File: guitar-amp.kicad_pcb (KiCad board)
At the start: 2 copper layers, 41 parts, among them U1 ECC81, U2 ECC81, U3 EL84

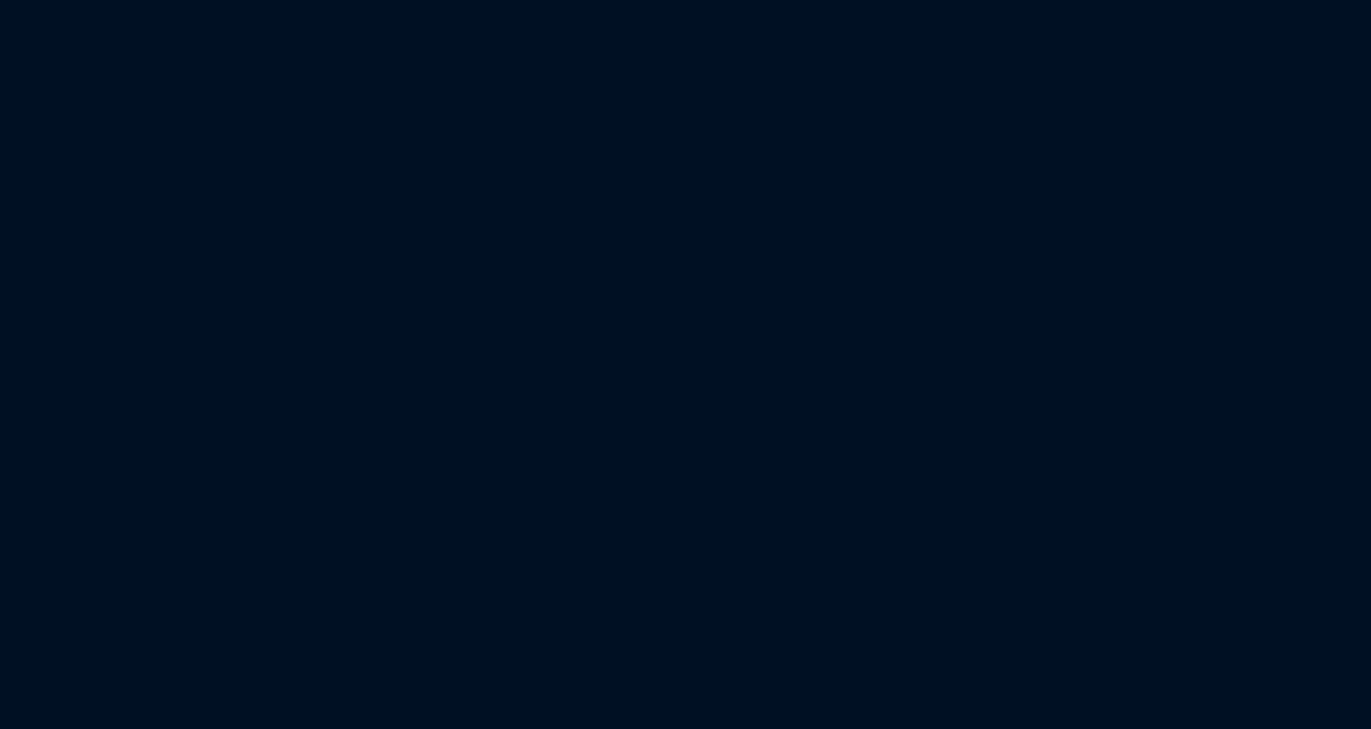
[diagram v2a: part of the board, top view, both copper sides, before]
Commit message: Add potentiometers
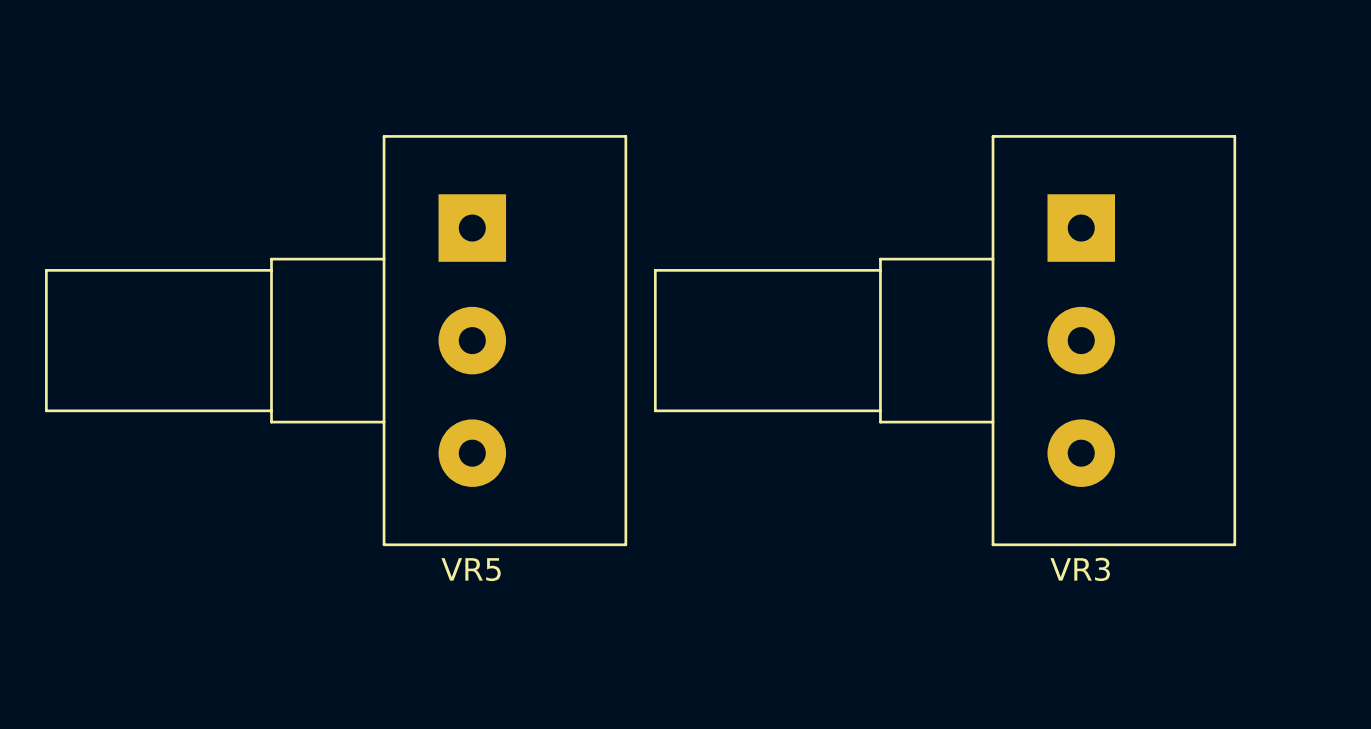
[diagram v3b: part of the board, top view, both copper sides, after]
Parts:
- added VR3: 220k LIN, Potentiometer_THT:Potentiometer_Alps_RK163_Single_Horizontal, F.Cu at (65.0, 70.0)
- added VR5: 25k LIN, Potentiometer_THT:Potentiometer_Alps_RK163_Single_Horizontal, F.Cu at (38.0, 70.0)
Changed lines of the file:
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@@
   (net 99 "unconnected-(C15-Pad1)")
   (net 100 "unconnected-(C15-Pad2)")
+  (net 101 "unconnected-(VR3-Pad1)")
+  (net 102 "unconnected-(VR3-Pad2)")
+  (net 103 "unconnected-(VR3-Pad3)")
+  (net 104 "unconnected-(VR5-Pad1)")
+  (net 105 "unconnected-(VR5-Pad2)")
+  (net 106 "unconnected-(VR5-Pad3)")
   (footprint "Resistor_THT:R_Axial_DIN0207_L6.3mm_D2.5mm_P7.62mm_Horizontal" (layer "F.Cu")
     (at 46.6 45.65)
@@
       (net 36 "unconnected-(R6-Pad2)") (pintype "passive"))
     (model "${KICAD6_3DMODEL_DIR}/Resistor_THT.3dshapes/R_Axial_DIN0207_L6.3mm_D2.5mm_P7.62mm_Horizontal.wrl"
+      (offset (xyz 0 0 0))
+      (scale (xyz 1 1 1))
+      (rotate (xyz 0 0 0))
+    )
+  )
+  (footprint "Potentiometer_THT:Potentiometer_Alps_RK163_Single_Horizontal" (layer "F.Cu")
+    (at 65 70)
+    (descr "1110U1Q 1110TNP 1110U2A 1110U0Q Potentiometer, horizontal, Alps RK163 Single, https://tech.alpsalpine.com/prod/e/pdf/potentiometer/rotarypotentiometers/rk16/rk16.pdf")
+    (tags "Potentiometer horizontal Alps RK163 Single")
+    (property "Sheetfile" "guitar-amp.kicad_sch")
+    (property "Sheetname" "")
+    (attr through_hole)
+    (fp_text reference "VR3" (at 0 15.2 180) (layer "F.SilkS")
+      (effects (font (size 1 1) (thickness 0.15)))
+    )
+    (fp_text value "220k LIN" (at 0 -5.200001 180) (layer "F.Fab")
+      (effects (font (size 1 1) (thickness 0.15)))
+    )
+    (fp_text user "${REFERENCE}" (at 1.45 4.999999 180) (layer "F.Fab")
+      (effects (font (size 1 1) (thickness 0.15)))
+    )
+    (fp_line (start -3.92 1.38) (end -8.92 1.38) (layer "F.SilkS") (width 0.12))
+    (fp_line (start -8.92 1.88) (end -18.92 1.88) (layer "F.SilkS") (width 0.12))
+    (fp_line (start 6.82 14.07) (end 6.82 -4.07) (layer "F.SilkS") (width 0.12))
+    (fp_line (start -3.92 14.07) (end -3.92 -4.07) (layer "F.SilkS") (width 0.12))
+    (fp_line (start -3.92 8.62) (end -8.92 8.62) (layer "F.SilkS") (width 0.12))
+    (fp_line (start 6.82 14.07) (end -3.92 14.07) (layer "F.SilkS") (width 0.12))
+    (fp_line (start -18.92 8.12) (end -18.92 1.88) (layer "F.SilkS") (width 0.12))
+    (fp_line (start -8.92 8.12) (end -18.92 8.12) (layer "F.SilkS") (width 0.12))
+    (fp_line (start 6.82 -4.07) (end -3.92 -4.07) (layer "F.SilkS") (width 0.12))
+    (fp_line (start -8.92 8.62) (end -8.92 1.38) (layer "F.SilkS") (width 0.12))
+    (fp_line (start -19.05 14.2) (end 6.95 14.2) (layer "F.CrtYd") (width 0.05))
+    (fp_line (start 6.95 -4.2) (end -19.05 -4.2) (layer "F.CrtYd") (width 0.05))
+    (fp_line (start 6.95 14.2) (end 6.95 -4.2) (layer "F.CrtYd") (width 0.05))
+    (fp_line (start -19.05 -4.2) (end -19.05 14.2) (layer "F.CrtYd") (width 0.05))
+    (fp_line (start -3.8 13.95) (end 6.7 13.95) (layer "F.Fab") (width 0.1))
+    (fp_line (start 6.7 -3.95) (end -3.8 -3.95) (layer "F.Fab") (width 0.1))
+    (fp_line (start -18.8 8) (end -8.8 8) (layer "F.Fab") (width 0.1))
+    (fp_line (start -3.8 -3.95) (end -3.8 13.95) (layer "F.Fab") (width 0.1))
+    (fp_line (start -18.8 2) (end -18.8 8) (layer "F.Fab") (width 0.1))
+    (fp_line (start -8.8 2) (end -18.8 2) (layer "F.Fab") (width 0.1))
+    (fp_line (start -8.8 1.5) (end -8.8 8.5) (layer "F.Fab") (width 0.1))
+    (fp_line (start -8.8 8.5) (end -3.8 8.5) (layer "F.Fab") (width 0.1))
+    (fp_line (start 6.7 13.95) (end 6.7 -3.95) (layer "F.Fab") (width 0.1))
+    (fp_line (start -3.8 1.5) (end -8.8 1.5) (layer "F.Fab") (width 0.1))
+    (pad "1" thru_hole rect (at 0 0 180) (size 3 3) (drill 1.2) (layers *.Cu *.Mask)
+      (net 101 "unconnected-(VR3-Pad1)") (pinfunction "1") (pintype "passive"))
+    (pad "2" thru_hole circle (at 0 5 180) (size 3 3) (drill 1.2) (layers *.Cu *.Mask)
+      (net 102 "unconnected-(VR3-Pad2)") (pinfunction "2") (pintype "passive"))
+    (pad "3" thru_hole circle (at 0 10 180) (size 3 3) (drill 1.2) (layers *.Cu *.Mask)
+      (net 103 "unconnected-(VR3-Pad3)") (pinfunction "3") (pintype "passive"))
+    (model "${KICAD6_3DMODEL_DIR}/Potentiometer_THT.3dshapes/Potentiometer_Alps_RK163_Single_Horizontal.wrl"
       (offset (xyz 0 0 0))
       (scale (xyz 1 1 1))
@@
       (offset (xyz 0 0 0))
       (scale (xyz 1 1 1))
+      (rotate (xyz 0 0 0))
+    )
+  )
+  (footprint "Potentiometer_THT:Potentiometer_Alps_RK163_Single_Horizontal" (layer "F.Cu")
+    (at 37.95 70)
+    (descr "1110U1Q 1110TNP 1110U2A 1110U0Q Potentiometer, horizontal, Alps RK163 Single, https://tech.alpsalpine.com/prod/e/pdf/potentiometer/rotarypotentiometers/rk16/rk16.pdf")
+    (tags "Potentiometer horizontal Alps RK163 Single")
+    (property "Sheetfile" "guitar-amp.kicad_sch")
+    (property "Sheetname" "")
+    (attr through_hole)
+    (fp_text reference "VR5" (at 0 15.2 180) (layer "F.SilkS")
+      (effects (font (size 1 1) (thickness 0.15)))
+    )
+    (fp_text value "25k LIN" (at 0 -5.200001 180) (layer "F.Fab")
+      (effects (font (size 1 1) (thickness 0.15)))
+    )
+    (fp_text user "${REFERENCE}" (at 1.45 4.999999 180) (layer "F.Fab")
+      (effects (font (size 1 1) (thickness 0.15)))
+    )
+    (fp_line (start -3.92 8.62) (end -8.92 8.62) (layer "F.SilkS") (width 0.12))
+    (fp_line (start -3.92 14.07) (end -3.92 -4.07) (layer "F.SilkS") (width 0.12))
+    (fp_line (start 6.82 -4.07) (end -3.92 -4.07) (layer "F.SilkS") (width 0.12))
+    (fp_line (start 6.82 14.07) (end 6.82 -4.07) (layer "F.SilkS") (width 0.12))
+    (fp_line (start -8.92 8.12) (end -18.92 8.12) (layer "F.SilkS") (width 0.12))
+    (fp_line (start -3.92 1.38) (end -8.92 1.38) (layer "F.SilkS") (width 0.12))
+    (fp_line (start -18.92 8.12) (end -18.92 1.88) (layer "F.SilkS") (width 0.12))
+    (fp_line (start -8.92 1.88) (end -18.92 1.88) (layer "F.SilkS") (width 0.12))
+    (fp_line (start -8.92 8.62) (end -8.92 1.38) (layer "F.SilkS") (width 0.12))
+    (fp_line (start 6.82 14.07) (end -3.92 14.07) (layer "F.SilkS") (width 0.12))
+    (fp_line (start -19.05 -4.2) (end -19.05 14.2) (layer "F.CrtYd") (width 0.05))
+    (fp_line (start 6.95 14.2) (end 6.95 -4.2) (layer "F.CrtYd") (width 0.05))
+    (fp_line (start -19.05 14.2) (end 6.95 14.2) (layer "F.CrtYd") (width 0.05))
+    (fp_line (start 6.95 -4.2) (end -19.05 -4.2) (layer "F.CrtYd") (width 0.05))
+    (fp_line (start -3.8 -3.95) (end -3.8 13.95) (layer "F.Fab") (width 0.1))
+    (fp_line (start 6.7 -3.95) (end -3.8 -3.95) (layer "F.Fab") (width 0.1))
+    (fp_line (start -3.8 13.95) (end 6.7 13.95) (layer "F.Fab") (width 0.1))
+    (fp_line (start -8.8 2) (end -18.8 2) (layer "F.Fab") (width 0.1))
+    (fp_line (start -18.8 8) (end -8.8 8) (layer "F.Fab") (width 0.1))
+    (fp_line (start -18.8 2) (end -18.8 8) (layer "F.Fab") (width 0.1))
+    (fp_line (start -3.8 1.5) (end -8.8 1.5) (layer "F.Fab") (width 0.1))
+    (fp_line (start -8.8 1.5) (end -8.8 8.5) (layer "F.Fab") (width 0.1))
+    (fp_line (start -8.8 8.5) (end -3.8 8.5) (layer "F.Fab") (width 0.1))
+    (fp_line (start 6.7 13.95) (end 6.7 -3.95) (layer "F.Fab") (width 0.1))
+    (pad "1" thru_hole rect (at 0 0 180) (size 3 3) (drill 1.2) (layers *.Cu *.Mask)
+      (net 104 "unconnected-(VR5-Pad1)") (pinfunction "1") (pintype "passive"))
+    (pad "2" thru_hole circle (at 0 5 180) (size 3 3) (drill 1.2) (layers *.Cu *.Mask)
+      (net 105 "unconnected-(VR5-Pad2)") (pinfunction "2") (pintype "passive"))
+    (pad "3" thru_hole circle (at 0 10 180) (size 3 3) (drill 1.2) (layers *.Cu *.Mask)
+      (net 106 "unconnected-(VR5-Pad3)") (pinfunction "3") (pintype "passive"))
+    (model "${KICAD6_3DMODEL_DIR}/Potentiometer_THT.3dshapes/Potentiometer_Alps_RK163_Single_Horizontal.wrl"
+      (offset (xyz 0 0 0))
+      (scale (xyz 1 1 1))

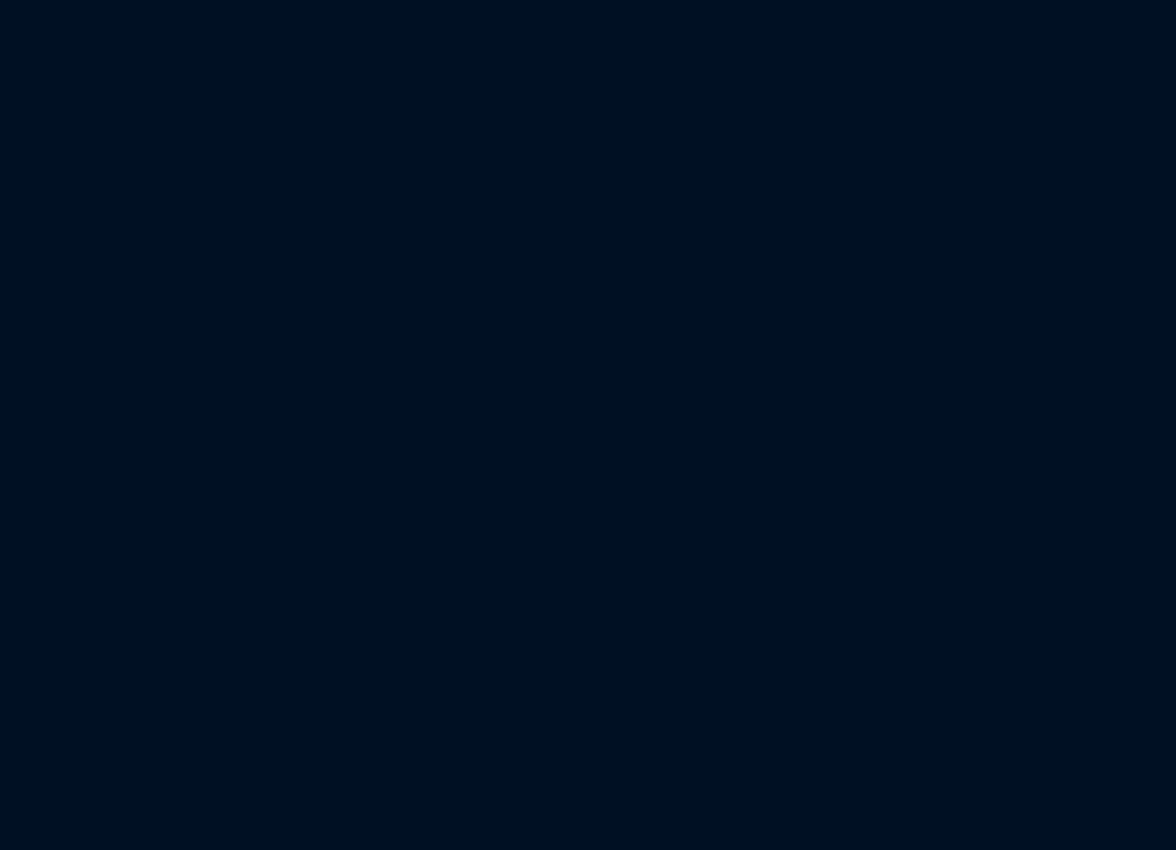
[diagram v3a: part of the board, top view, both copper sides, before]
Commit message: Add guitar jack
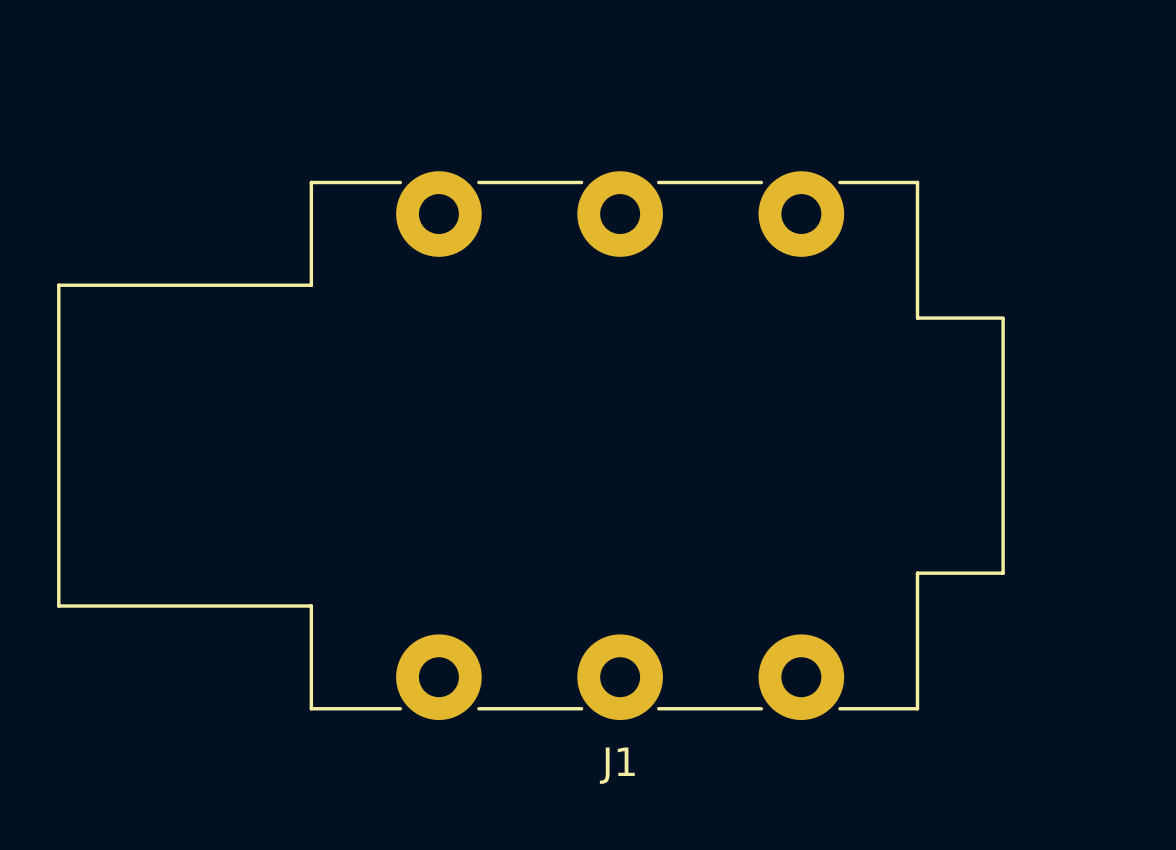
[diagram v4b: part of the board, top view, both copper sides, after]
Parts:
- added J1: AudioJack3_Switch, Connector_Audio:Jack_6.35mm_Neutrik_NMJ6HFD2-AU_Horizontal, F.Cu at (16.9, 109.8)
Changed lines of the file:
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@@
   (net 105 "unconnected-(VR5-Pad2)")
   (net 106 "unconnected-(VR5-Pad3)")
+  (net 107 "unconnected-(J1-PadR)")
+  (net 108 "unconnected-(J1-PadRN)")
+  (net 109 "GND")
+  (net 110 "unconnected-(J1-PadT)")
+  (net 111 "unconnected-(J1-PadTN)")
   (footprint "Resistor_THT:R_Axial_DIN0207_L6.3mm_D2.5mm_P7.62mm_Horizontal" (layer "F.Cu")
     (at 46.6 45.65)
@@
     )
   )
+  (footprint "Connector_Audio:Jack_6.35mm_Neutrik_NMJ6HFD2-AU_Horizontal" (layer "F.Cu")
+    (at 16.925 109.765 180)
+    (descr "M Series, 6.35mm (1/4in) stereo jack, switched, full threaded nose, straight PCB pins, gold plated contacts, https://www.neutrik.com/en/product/nmj6hfd2-au")
+    (tags "neutrik jack m")
+    (property "Sheetfile" "guitar-amp.kicad_sch")
+    (property "Sheetname" "")
+    (attr through_hole)
+    (fp_text reference "J1" (at 6.35 -3) (layer "F.SilkS")
+      (effects (font (size 1 1) (thickness 0.15)))
+    )
+    (fp_text value "AudioJack3_Switch" (at 6.35 19) (layer "F.Fab")
+      (effects (font (size 1 1) (thickness 0.15)))
+    )
+    (fp_text user "${REFERENCE}" (at 6.35 8.115) (layer "F.Fab")
+      (effects (font (size 1 1) (thickness 0.15)))
+    )
+    (fp_line (start 7.7 -1.105) (end 11.3 -1.105) (layer "F.SilkS") (width 0.12))
+    (fp_line (start 11.3 17.335) (end 7.7 17.335) (layer "F.SilkS") (width 0.12))
+    (fp_line (start 17.17 17.335) (end 14.05 17.335) (layer "F.SilkS") (width 0.12))
+    (fp_line (start 17.17 -1.105) (end 14.05 -1.105) (layer "F.SilkS") (width 0.12))
+    (fp_line (start 17.17 2.495) (end 26.02 2.495) (layer "F.SilkS") (width 0.12))
+    (fp_line (start -4.07 17.335) (end -4.07 12.585) (layer "F.SilkS") (width 0.12))
+    (fp_line (start 17.17 17.335) (end 17.17 13.735) (layer "F.SilkS") (width 0.12))
+    (fp_line (start -4.07 -1.105) (end -1.35 -1.105) (layer "F.SilkS") (width 0.12))
+    (fp_line (start 17.17 2.495) (end 17.17 -1.105) (layer "F.SilkS") (width 0.12))
+    (fp_line (start -7.07 12.585) (end -4.07 12.585) (layer "F.SilkS") (width 0.12))
+    (fp_line (start 26.02 13.735) (end 26.02 2.495) (layer "F.SilkS") (width 0.12))
+    (fp_line (start -1.35 17.335) (end -4.07 17.335) (layer "F.SilkS") (width 0.12))
+    (fp_line (start -4.07 3.645) (end -4.07 -1.105) (layer "F.SilkS") (width 0.12))
+    (fp_line (start -7.07 3.645) (end -4.07 3.645) (layer "F.SilkS") (width 0.12))
+    (fp_line (start 17.17 13.735) (end 26.02 13.735) (layer "F.SilkS") (width 0.12))
+    (fp_line (start -7.07 12.545) (end -7.07 3.645) (layer "F.SilkS") (width 0.12))
+    (fp_line (start 5 17.335) (end 1.4 17.335) (layer "F.SilkS") (width 0.12))
+    (fp_line (start 1.4 -1.105) (end 5 -1.105) (layer "F.SilkS") (width 0.12))
+    (fp_line (start 26.4 -2) (end -7.45 -2) (layer "F.CrtYd") (width 0.05))
+    (fp_line (start -7.45 18.23) (end 26.4 18.23) (layer "F.CrtYd") (width 0.05))
+    (fp_line (start -7.45 18.23) (end -7.45 -2) (layer "F.CrtYd") (width 0.05))
+    (fp_line (start 26.4 18.23) (end 26.4 -2) (layer "F.CrtYd") (width 0.05))
+    (fp_line (start -6.95 12.465) (end -3.95 12.465) (layer "F.Fab") (width 0.1))
+    (fp_line (start 17.05 17.215) (end -3.95 17.215) (layer "F.Fab") (width 0.1))
+    (fp_line (start 25.9 2.615) (end 17.05 2.615) (layer "F.Fab") (width 0.1))
+    (fp_line (start 17.05 -0.985) (end -3.95 -0.985) (layer "F.Fab") (width 0.1))
+    (fp_line (start -6.95 12.465) (end -6.95 3.765) (layer "F.Fab") (width 0.1))
+    (fp_line (start 17.05 17.215) (end 17.05 -0.985) (layer "F.Fab") (width 0.1))
+    (fp_line (start 25.9 13.615) (end 17.05 13.615) (layer "F.Fab") (width 0.1))
+    (fp_line (start -3.95 17.215) (end -3.95 -0.985) (layer "F.Fab") (width 0.1))
+    (fp_line (start -6.95 3.765) (end -3.95 3.765) (layer "F.Fab") (width 0.1))
+    (fp_line (start 25.9 13.615) (end 25.9 2.615) (layer "F.Fab") (width 0.1))
+    (pad "R" thru_hole circle (at 6.35 0 180) (size 3 3) (drill 1.4) (layers *.Cu *.Mask)
+      (net 107 "unconnected-(J1-PadR)") (pintype "passive"))
+    (pad "RN" thru_hole circle (at 6.35 16.23 180) (size 3 3) (drill 1.4) (layers *.Cu *.Mask)
+      (net 108 "unconnected-(J1-PadRN)") (pintype "passive"))
+    (pad "S" thru_hole circle (at 12.7 0 180) (size 3 3) (drill 1.4) (layers *.Cu *.Mask)
+      (net 109 "GND") (pintype "passive"))
+    (pad "SN" thru_hole circle (at 12.7 16.23 180) (size 3 3) (drill 1.4) (layers *.Cu *.Mask)
+      (net 109 "GND") (pintype "passive"))
+    (pad "T" thru_hole circle (at 0 0 180) (size 3 3) (drill 1.4) (layers *.Cu *.Mask)
+      (net 110 "unconnected-(J1-PadT)") (pintype "passive"))
+    (pad "TN" thru_hole circle (at 0 16.23 180) (size 3 3) (drill 1.4) (layers *.Cu *.Mask)
+      (net 111 "unconnected-(J1-PadTN)") (pintype "passive"))
+    (model "${KICAD6_3DMODEL_DIR}/Connector_Audio.3dshapes/Jack_6.35mm_Neutrik_NMJ6HFD2-AU_Horizontal.wrl"
+      (offset (xyz 0 0 0))
+      (scale (xyz 1 1 1))
+      (rotate (xyz 0 0 0))
+    )
+    (model "${KIPRJMOD}/lib/nmj6hcd3.step"
+      (offset (xyz 15.5 -8 1.5))
+      (scale (xyz 1 1 1))
+      (rotate (xyz -90 0 -90))
+    )
+  )
